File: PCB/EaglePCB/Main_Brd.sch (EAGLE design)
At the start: 80 parts, among them U1 ATWINC1500-MR210PB1952-T, U3 MSP430FR2355TDBTRDBT0038A_M, U6 ARJM11C7-114-BA-EW2

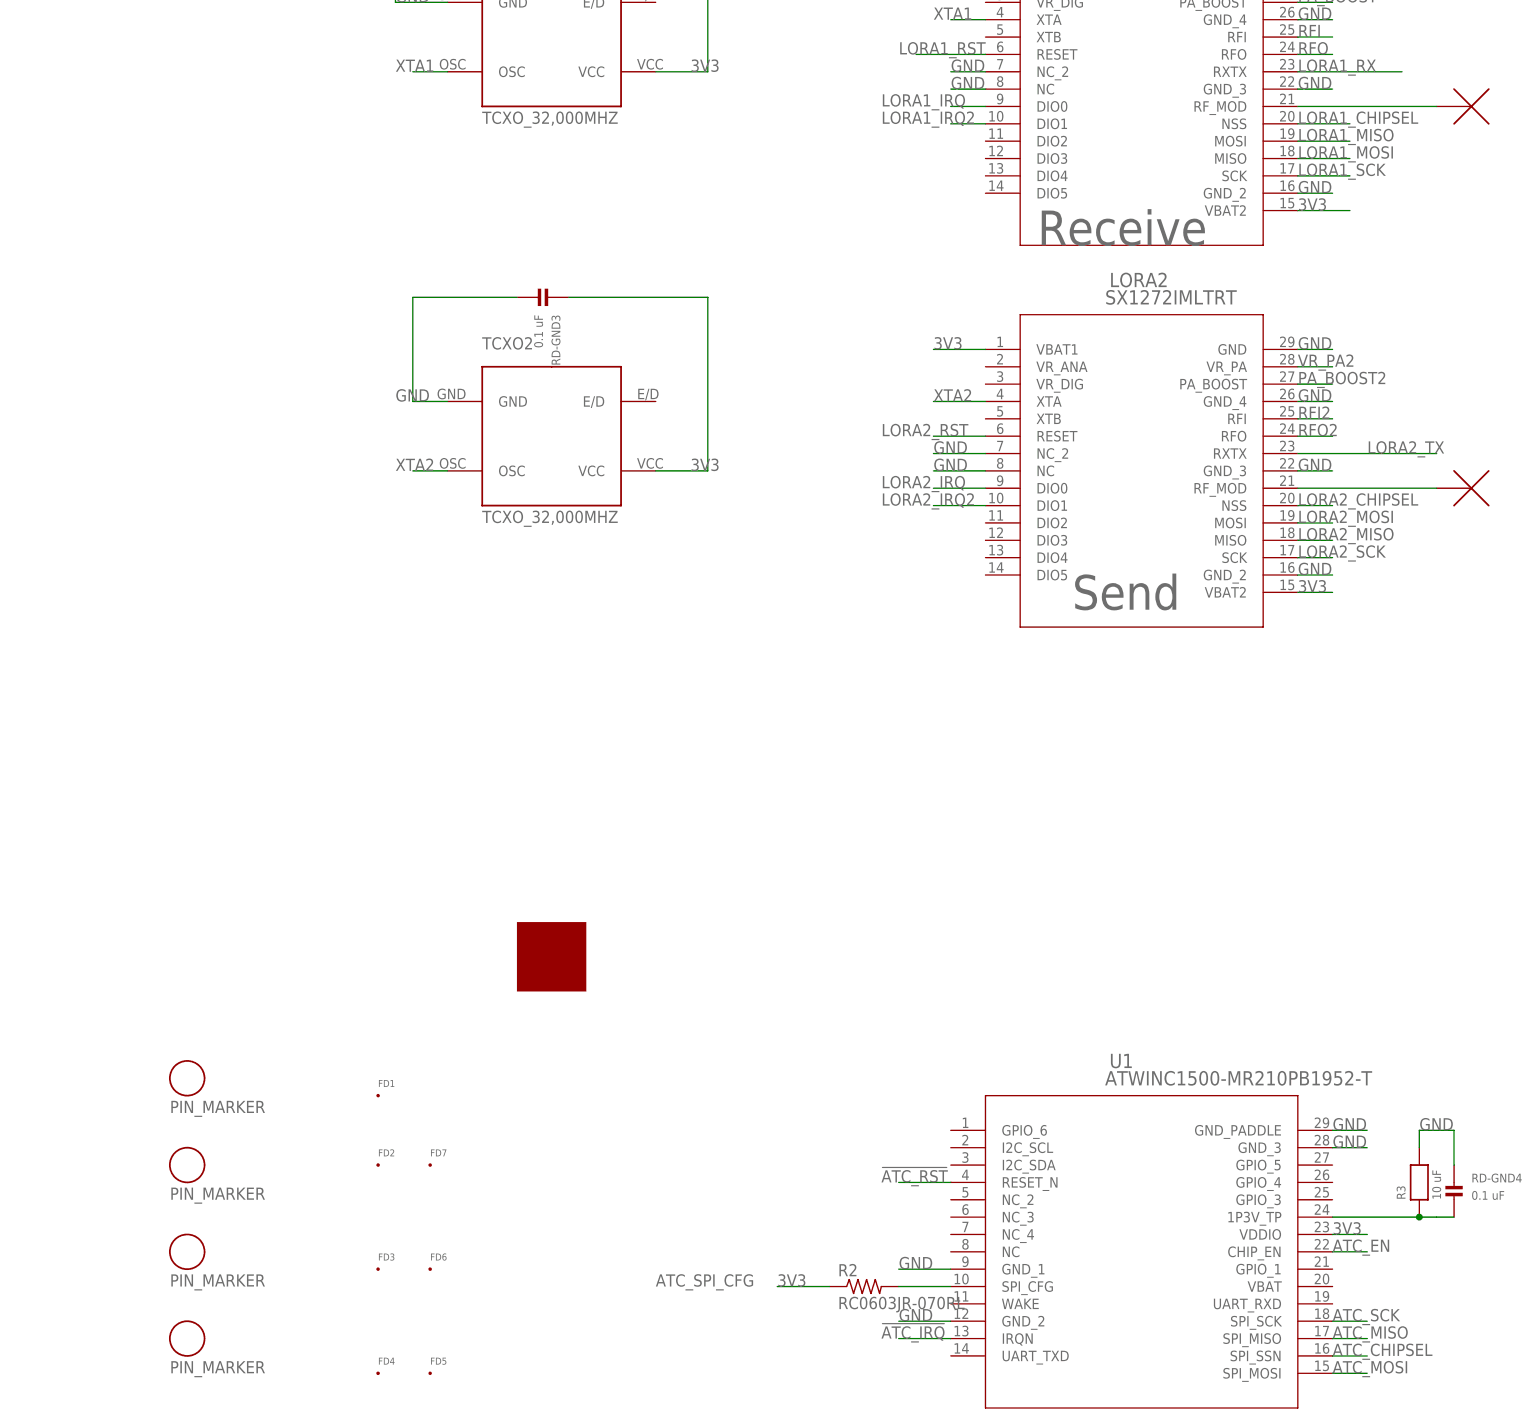
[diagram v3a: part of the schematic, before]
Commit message: EaglePCB Changes: - Converted 4 layer to 2 layer for cost savings - Removed Fiducials for simplicity - Switched MOSI/MISO on LoRa1 for correctness
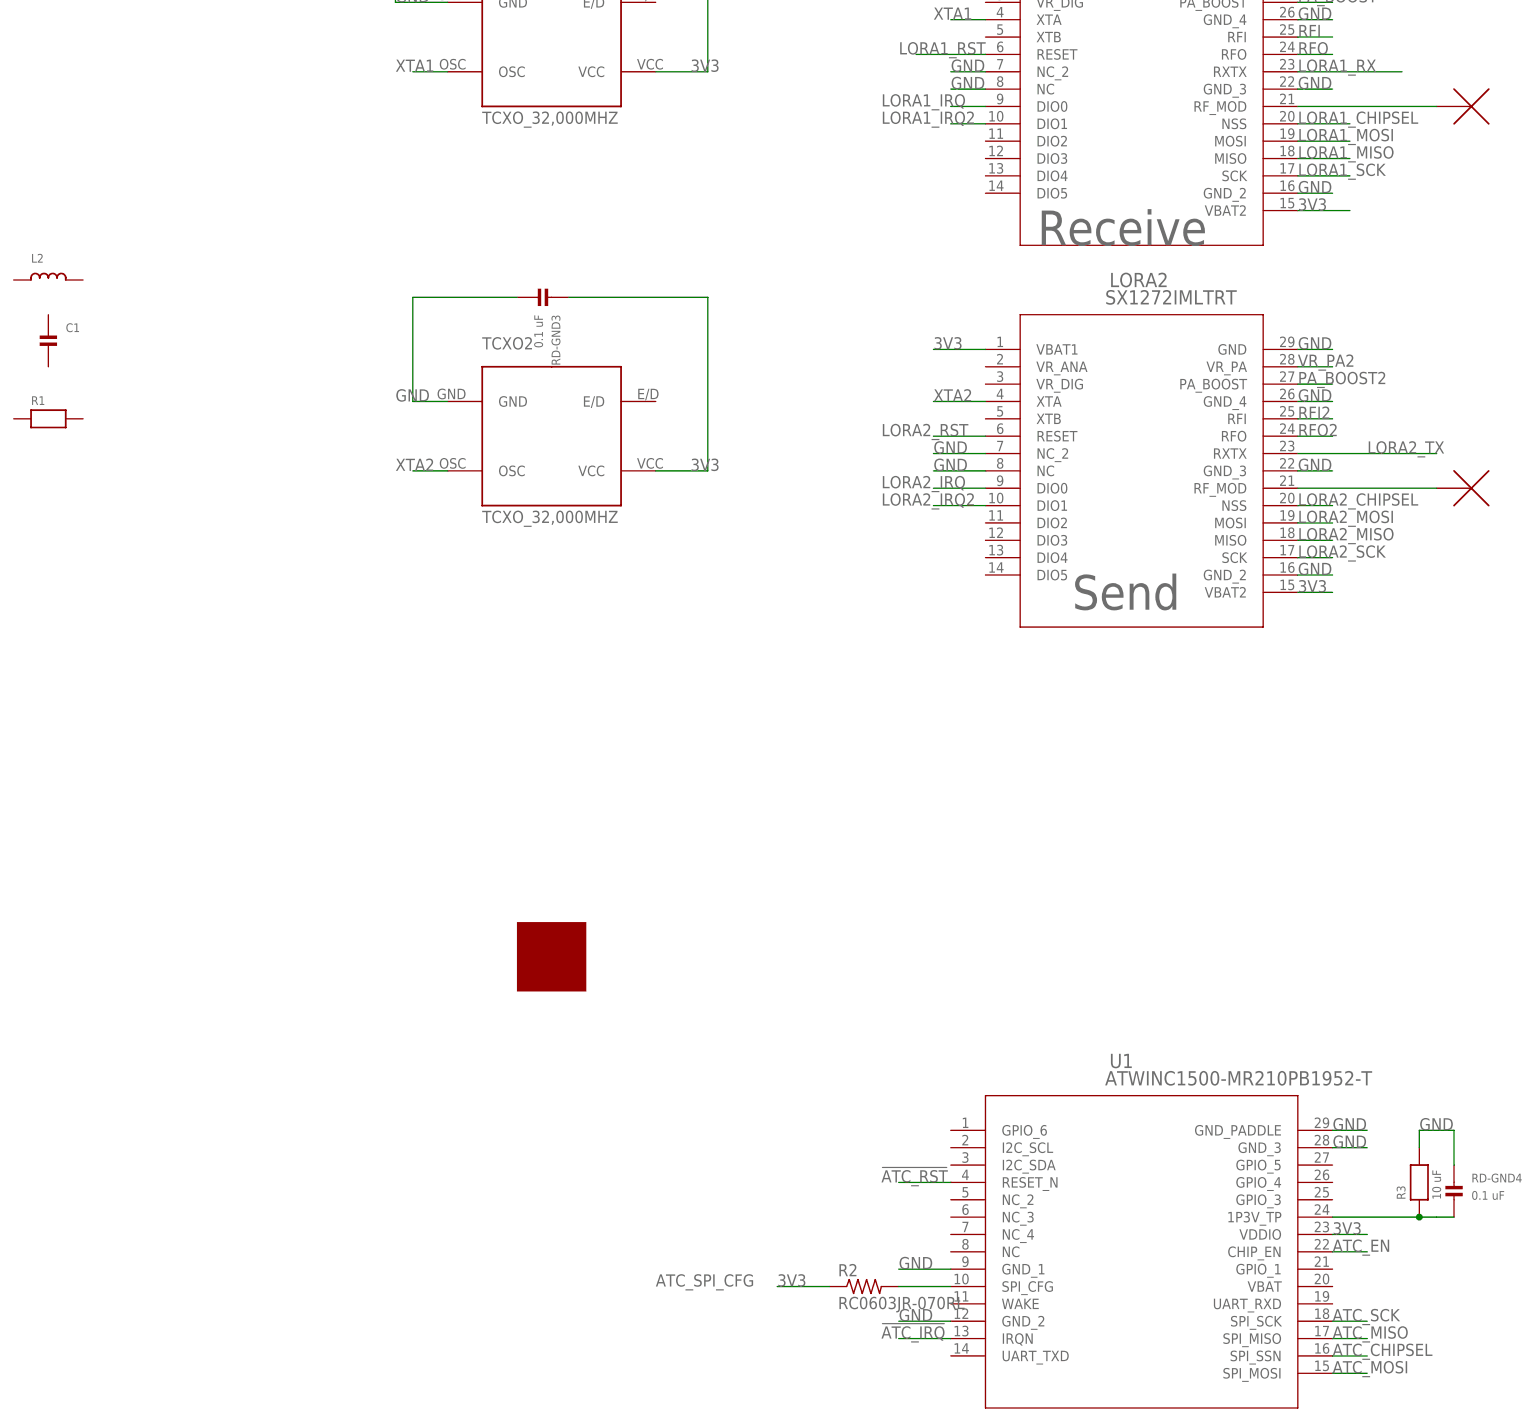
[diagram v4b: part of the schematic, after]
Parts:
- removed FD1, FD2, FD3, FD4, FD5, FD6, FD7: FID_40MIL, Fiducial:FID_40MIL
- removed U$10, U$11, U$12, U$9: PIN_MARKER, 473:PIN_MARKER
- added C1: (no value), microbuilder:CAP_CERAMIC0402
- added L2: (no value), microbuilder:INDUCTOR_0402
- added R1: (no value), microbuilder:RESISTOR0402
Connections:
- net LORA1_MISO: now also LORA1.MISO; no longer LORA1.MOSI
- net LORA1_MOSI: now also LORA1.MOSI; no longer LORA1.MISO
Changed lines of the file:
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@@
 <?xml version="1.0" encoding="utf-8"?>
 <!DOCTYPE eagle SYSTEM "eagle.dtd">
-<eagle version="9.6.2">
+<eagle version="9.7.0">
 <drawing>
 <settings>
@@
 <layer number="59" name="tCarbon" color="7" fill="1" visible="no" active="no"/>
 <layer number="60" name="bCarbon" color="7" fill="1" visible="no" active="no"/>
-<layer number="88" name="SimResults" color="9" fill="1" visible="no" active="yes"/>
+<layer number="88" name="SimResults" color="9" fill="1" visible="yes" active="yes"/>
 <layer number="89" name="SimProbes" color="9" fill="1" visible="yes" active="yes"/>
 <layer number="90" name="Modules" color="5" fill="1" visible="yes" active="yes"/>
@@
 <part name="VR_PA-PA_BOOST" library="microbuilder" deviceset="INDUCTOR" device="_0402" value="33nH"/>
 <part name="RFO-33PF" library="microbuilder" deviceset="INDUCTOR" device="_0402" value="10nH"/>
+<part name="L2" library="microbuilder" deviceset="INDUCTOR" device="_0402"/>
+<part name="C1" library="microbuilder" deviceset="CAP_CERAMIC" device="0402"/>
+<part name="R1" library="microbuilder" deviceset="RESISTOR" device="0402"/>
 <part name="10NH-ANT1" library="microbuilder" deviceset="CAP_CERAMIC" device="0402"/>
 <part name="ANT1-GND" library="microbuilder" deviceset="CAP_CERAMIC" device="0402" value="4.7pF"/>
@@
 <part name="U$7" library="473" deviceset="BARREL_CONN_EXTERN" device=""/>
 <part name="U$8" library="473" library_urn="urn:adsk.wipprod:fs.file:vf.lBtoW6XlTqmMxyMuKqhWUA" deviceset="MAGICWIFI_X10" device="" value="MAGICWIFI_X10"/>
-<part name="U$9" library="473" deviceset="PIN_MARKER" device=""/>
-<part name="U$10" library="473" deviceset="PIN_MARKER" device=""/>
-<part name="U$11" library="473" deviceset="PIN_MARKER" device=""/>
-<part name="U$12" library="473" deviceset="PIN_MARKER" device=""/>
-<part name="FD1" library="Fiducial" deviceset="FID" device="_40MIL"/>
-<part name="FD2" library="Fiducial" deviceset="FID" device="_40MIL"/>
-<part name="FD3" library="Fiducial" deviceset="FID" device="_40MIL"/>
-<part name="FD4" library="Fiducial" deviceset="FID" device="_40MIL"/>
-<part name="FD5" library="Fiducial" deviceset="FID" device="_40MIL"/>
-<part name="FD6" library="Fiducial" deviceset="FID" device="_40MIL"/>
-<part name="FD7" library="Fiducial" deviceset="FID" device="_40MIL"/>
 </parts>
 <sheets>
@@
 <attribute name="VALUE" x="-40.64" y="195.58" size="1.27" layer="96"/>
 </instance>
+<instance part="L2" gate="G$1" x="-210.82" y="55.88" smashed="yes" grouprefs="0402">
+<attribute name="NAME" x="-213.36" y="58.42" size="1.27" layer="95"/>
+<attribute name="VALUE" x="-213.36" y="53.34" size="1.27" layer="96"/>
+</instance>
+<instance part="C1" gate="G$1" x="-210.82" y="45.72" smashed="yes" grouprefs="0402">
+<attribute name="NAME" x="-208.28" y="48.26" size="1.27" layer="95" font="vector"/>
+<attribute name="VALUE" x="-208.28" y="45.72" size="1.27" layer="96" font="vector"/>
+</instance>
+<instance part="R1" gate="G$1" x="-210.82" y="35.56" smashed="yes" grouprefs="0402">
+<attribute name="NAME" x="-213.36" y="37.592" size="1.27" layer="95" font="vector"/>
+<attribute name="VALUE" x="-213.36" y="32.385" size="1.27" layer="96" font="vector"/>
+</instance>
 <instance part="10NH-ANT1" gate="G$1" x="-50.8" y="198.12" smashed="yes" rot="R90" grouprefs="ANTENNA1">
 <attribute name="NAME" x="-53.34" y="200.66" size="1.27" layer="95" font="vector" rot="R90"/>
@@
 <instance part="U$7" gate="G$1" x="101.6" y="91.44" smashed="yes"/>
 <instance part="U$8" gate="G$1" x="-137.16" y="-43.18" smashed="yes"/>
-<instance part="U$9" gate="G$1" x="-190.5" y="-60.96" smashed="yes">
-<attribute name="VALUE" x="-193.04" y="-66.04" size="1.778" layer="96"/>
-</instance>
-<instance part="U$10" gate="G$1" x="-190.5" y="-73.66" smashed="yes">
-<attribute name="VALUE" x="-193.04" y="-78.74" size="1.778" layer="96"/>
-</instance>
-<instance part="U$11" gate="G$1" x="-190.5" y="-86.36" smashed="yes">
-<attribute name="VALUE" x="-193.04" y="-91.44" size="1.778" layer="96"/>
-</instance>
-<instance part="U$12" gate="G$1" x="-190.5" y="-99.06" smashed="yes">
-<attribute name="VALUE" x="-193.04" y="-104.14" size="1.778" layer="96"/>
-</instance>
-<instance part="FD1" gate="G$2" x="-162.56" y="-63.5" smashed="yes">
-<attribute name="NAME" x="-162.56" y="-62.23" size="1.016" layer="95" font="vector" ratio="12"/>
-</instance>
-<instance part="FD2" gate="G$2" x="-162.56" y="-73.66" smashed="yes">
-<attribute name="NAME" x="-162.56" y="-72.39" size="1.016" layer="95" font="vector" ratio="12"/>
-</instance>
-<instance part="FD3" gate="G$2" x="-162.56" y="-88.9" smashed="yes">
-<attribute name="NAME" x="-162.56" y="-87.63" size="1.016" layer="95" font="vector" ratio="12"/>
-</instance>
-<instance part="FD4" gate="G$2" x="-162.56" y="-104.14" smashed="yes">
-<attribute name="NAME" x="-162.56" y="-102.87" size="1.016" layer="95" font="vector" ratio="12"/>
-</instance>
-<instance part="FD5" gate="G$2" x="-154.94" y="-104.14" smashed="yes">
-<attribute name="NAME" x="-154.94" y="-102.87" size="1.016" layer="95" font="vector" ratio="12"/>
-</instance>
-<instance part="FD6" gate="G$2" x="-154.94" y="-88.9" smashed="yes">
-<attribute name="NAME" x="-154.94" y="-87.63" size="1.016" layer="95" font="vector" ratio="12"/>
-</instance>
-<instance part="FD7" gate="G$2" x="-154.94" y="-73.66" smashed="yes">
-<attribute name="NAME" x="-154.94" y="-72.39" size="1.016" layer="95" font="vector" ratio="12"/>
-</instance>
 </instances>
 <busses>
@@
 <net name="LORA1_MISO" class="0">
 <segment>
+<pinref part="U3" gate="A" pin="P4.7_UCB1SOMI_UCB1SCL"/>
+<wire x1="182.88" y1="-81.28" x2="190.5" y2="-81.28" width="0.1524" layer="91"/>
+<label x="182.88" y="-81.28" size="1.778" layer="95"/>
+</segment>
+<segment>
+<pinref part="LORA1" gate="A" pin="MISO"/>
+<wire x1="-27.94" y1="73.66" x2="-20.32" y2="73.66" width="0.1524" layer="91"/>
+<label x="-27.94" y="73.66" size="1.778" layer="95"/>
+</segment>
+</net>
+<net name="LORA1_MOSI" class="0">
+<segment>
+<pinref part="U3" gate="A" pin="P4.6_UCB1SIMO_UCB1SDA"/>
+<wire x1="182.88" y1="-78.74" x2="193.04" y2="-78.74" width="0.1524" layer="91"/>
+<label x="182.88" y="-78.74" size="1.778" layer="95"/>
+</segment>
+<segment>
 <pinref part="LORA1" gate="A" pin="MOSI"/>
 <wire x1="-27.94" y1="76.2" x2="-20.32" y2="76.2" width="0.1524" layer="91"/>
 <label x="-27.94" y="76.2" size="1.778" layer="95"/>
 </segment>
-<segment>
-<pinref part="U3" gate="A" pin="P4.7_UCB1SOMI_UCB1SCL"/>
-<wire x1="182.88" y1="-81.28" x2="190.5" y2="-81.28" width="0.1524" layer="91"/>
-<label x="182.88" y="-81.28" size="1.778" layer="95"/>
-</segment>
-</net>
-<net name="LORA1_MOSI" class="0">
-<segment>
-<pinref part="LORA1" gate="A" pin="MISO"/>
-<wire x1="-27.94" y1="73.66" x2="-20.32" y2="73.66" width="0.1524" layer="91"/>
-<label x="-27.94" y="73.66" size="1.778" layer="95"/>
-</segment>
-<segment>
-<pinref part="U3" gate="A" pin="P4.6_UCB1SIMO_UCB1SDA"/>
-<wire x1="182.88" y1="-78.74" x2="193.04" y2="-78.74" width="0.1524" layer="91"/>
-<label x="182.88" y="-78.74" size="1.778" layer="95"/>
-</segment>
-</net>
+</net>

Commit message: Connected VBatt to 3v3 ATWinC
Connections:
- net 3V3: now also U1.VBAT
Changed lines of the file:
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@@
 <label x="124.46" y="91.44" size="1.778" layer="95"/>
+</segment>
+<segment>
+<pinref part="U1" gate="A" pin="VBAT"/>
+<wire x1="-22.86" y1="-91.44" x2="-17.78" y2="-91.44" width="0.1524" layer="91"/>
+<label x="-22.86" y="-91.44" size="1.778" layer="95"/>
 </segment>
 </net>
